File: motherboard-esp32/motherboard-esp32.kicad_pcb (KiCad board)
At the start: 4 copper layers, 123.8 x 77 mm, 41 parts, among them J2 Screw_Terminal_01x02, J3 JST_2P_XH, J4 JST_2P_XH, J5 Screw_Terminal_01x02, J6 Screw_Terminal_01x02, J7 XT60, P1 1.8mm_16AWG, P2 1.8mm_16AWG, P3 1.8mm_16AWG, P4 1.8mm_16AWG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

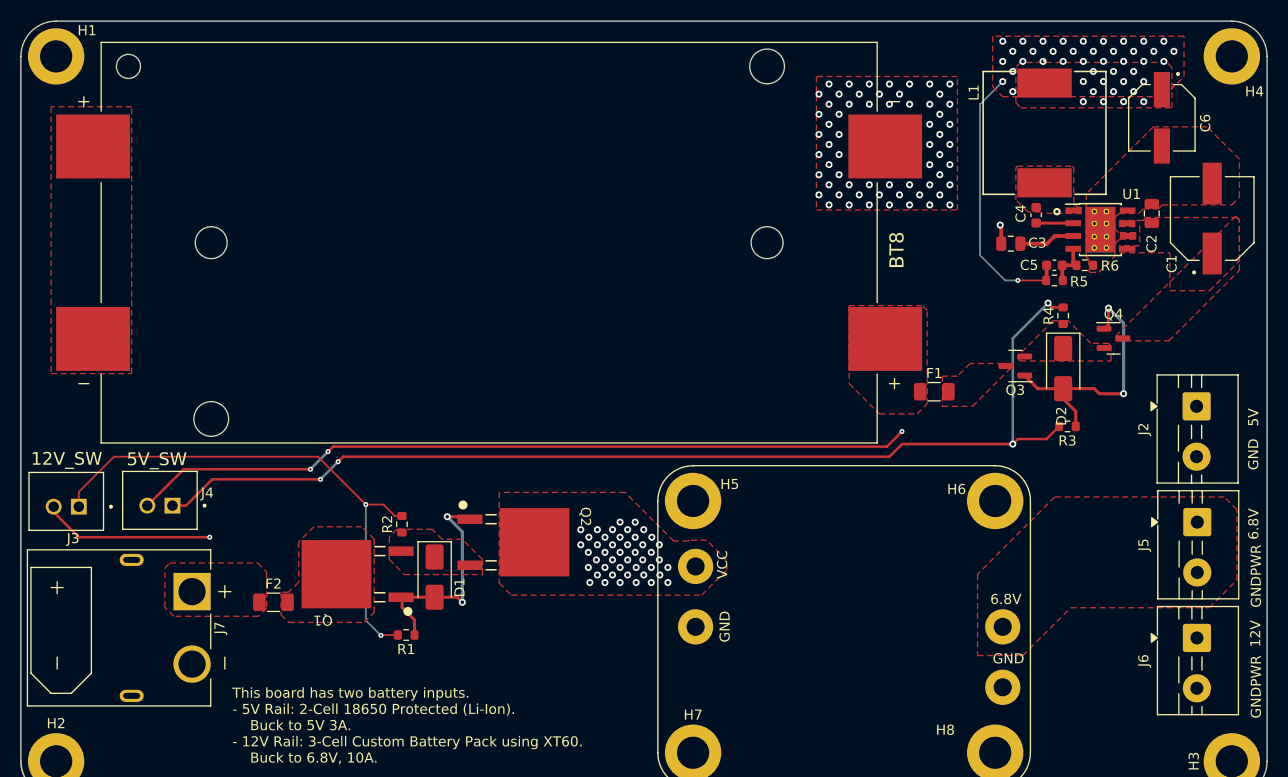
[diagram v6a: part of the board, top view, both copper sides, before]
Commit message: 5V 5A version
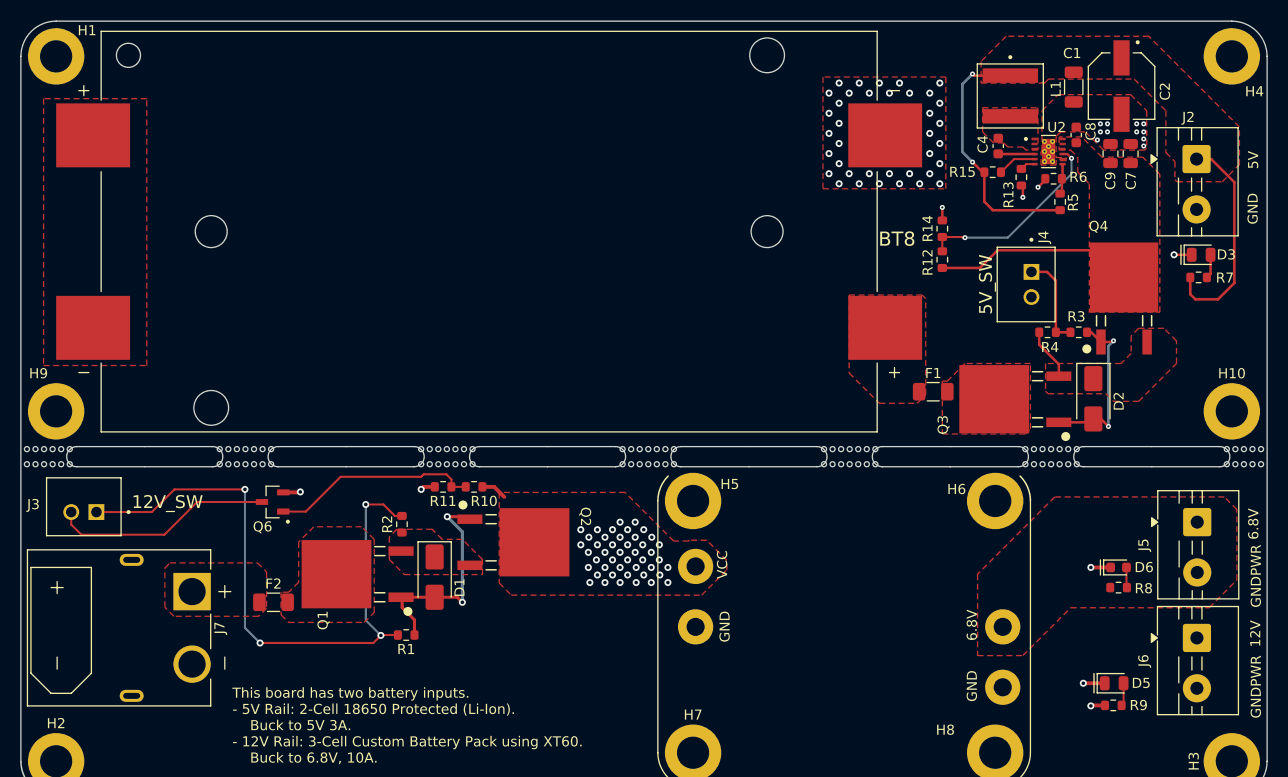
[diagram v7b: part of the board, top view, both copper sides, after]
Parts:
- removed C3: 2.2u, bio-robot:C_0805_2012Metric
- removed C5: 30p, bio-robot:C_0603_1608Metric
- removed C6: 16SVPF180M, bio-robot:CAP_16SVPF180M
- removed U1: LMR23630AFDDAR, bio-robot:TI_SO-PowerPAD-8_ThermalVias
- added B1: MouseBite, bio-robot:MouseBite-Long, F.Cu at (52.8, 61.8)
- added C7: 10u, bio-robot:C_0805_2012Metric, F.Cu at (160.7, 30.6)
- added C8: 0.1u, bio-robot:C_0603_1608Metric, F.Cu at (155.3, 28.8)
- added C9: 10u, bio-robot:C_0805_2012Metric, F.Cu at (158.7, 30.6)
- added D3: LED_green, bio-robot:LED_0805_2012Metric, F.Cu at (167.7, 40.7)
- added D5: LED_red, bio-robot:LED_0805_2012Metric, F.Cu at (159.1, 83.2)
- added D6: LED_blue, bio-robot:LED_0603_1608Metric, F.Cu at (159.5, 71.8)
- added H10: MountingHoleM3, bio-robot:MountingHole_3.2mm_M3_DIN965_Pad, F.Cu at (170.8, 56.2)
- added H9: MountingHoleM3, bio-robot:MountingHole_3.2mm_M3_DIN965_Pad, F.Cu at (54.0, 56.2)
- added Q6: TN2130K1-G, bio-robot:SOT95P240X111-3N, F.Cu at (75.5, 65.2)
- added R10: 11k, bio-robot:R_0603_1608Metric, F.Cu at (95.5, 63.8)
- added R11: 3.6k, bio-robot:R_0603_1608Metric, F.Cu at (92.4, 63.8)
- added R12: 698k, bio-robot:R_0603_1608Metric, F.Cu at (142.0, 41.2)
- added R13: 30.9k, bio-robot:R_0603_1608Metric, F.Cu at (149.8, 33.0)
- added R14: 200k, bots:R_0603_1608Metric, F.Cu at (142.0, 38.1)
- added R15: 100k, bots:R_0603_1608Metric, F.Cu at (147.0, 32.5)
- added R7: 3.3k, bio-robot:R_0603_1608Metric, F.Cu at (167.4, 43.0)
- added R8: 2k, bio-robot:R_0603_1608Metric, F.Cu at (159.5, 73.8)
- added R9: R_34k, bio-robot:R_0603_1608Metric, F.Cu at (159.0, 85.4)
- added U2: LMR51450SDRRR, bio-robot:CONV_LMR51450SDRRR, F.Cu at (152.6, 30.4)
- C1: value 25SVPF100M -> 22u_1206; footprint bio-robot:CAP_25SVPF100M -> bio-robot:C_1206_3216Metric
- C2: value 10u -> 10SVPC120M; footprint bio-robot:C_0805_2012Metric -> bio-robot:CAP_10SVPC120MV
- L1: value 27uH -> 4.7u; footprint bio-robot:IND_CDRH127_LDNP-470MC_SUM -> bio-robot:IND_XAL6060-472MEC
- Q3, Q4: value HL3415A -> DOD4185; footprint bio-robot:SOT-23 -> bots:DPAK-3_ONS
- R5: value 88.7k -> 100k; footprint bio-robot:R_0603_1608Metric -> bots:R_0603_1608Metric
- R6: value 22.1k -> 19.1k
- moved J4 88.7 mm to (150.3, 43.6), turned to 90 degrees
- moved J2 24.6 mm to (167.2, 31.2)
- moved C1 19.0 mm to (155.1, 24.1), turned to -90 degrees
- moved C2 13.0 mm to (159.8, 23.9), turned to -90 degrees
- moved R3 9.42 mm to (155.6, 48.4)
- moved R6 9.13 mm to (153.1, 33.1), turned to 180 degrees
- moved C4 7.83 mm to (147.6, 29.9)
- moved R5 7.82 mm to (153.7, 35.5), turned to -90 degrees
- moved Q4 6.14 mm to (160.1, 43.0)
- moved L1 5.00 mm to (148.8, 24.9)
- moved D2 4.24 mm to (157.0, 55.0)
- moved Q3 3.91 mm to (147.2, 55.0), turned to 90 degrees
- moved R4 2.26 mm to (152.4, 48.4), turned to 0 degrees
- moved J3 1.82 mm to (56.8, 65.7)
- moved BT8 1.10 mm to (97.0, 38.4)
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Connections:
- C1 pad 1: +BATT -> +5V
- C2 pad 1: +BATT -> +5V
- J3 pad 2: GNDPWR -> /Power Input/LV_D_VCC
- Q3 pad 2: /Power Input/BAT5V_MID -> /Power Input/FUSE_BAT5V
- Q3 pad 3: /Power Input/FUSE_BAT5V -> /Power Input/BAT5V_MID
- Q4 pad 2: /Power Input/BAT5V_MID -> +BATT
- Q4 pad 3: +BATT -> /Power Input/BAT5V_MID
- R5 pad 1: +5V -> /dc-dc/FB
- R5 pad 2: /dc-dc/FB -> +5V
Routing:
- net /Power Input/SW2: track 108.4 -> 9.36 mm, vias 4 -> 0
- net GND: track 79.9 -> 5.36 mm, vias 66 -> 52
- net /Power Input/LV_D_VCC: track 0.00 -> 22.0 mm
- net /Power Input/LV_G_VCC: track 0.00 -> 20.6 mm
- net +5V: track 27.3 -> 47.4 mm, vias 45 -> 2
- net +BATT: track 0.00 -> 19.9 mm
- net /dc-dc/EN: track 0.00 -> 19.5 mm, vias 0 -> 2
- net /Power Input/SW: track 52.8 -> 63.2 mm, vias 2 -> 4
- net GNDPWR: track 17.1 -> 7.25 mm, vias 1 -> 4
- net /Power Input/VGATE_2: track 26.2 -> 17.2 mm
- net /dc-dc/U1_VCC: track 5.57 -> 0.00 mm
- net /Power Input/BAT5V_MID: track 0.00 -> 5.16 mm
- net VCC: track 0.00 -> 4.01 mm, vias 45 -> 46
- net /dc-dc/PG: track 0.00 -> 3.87 mm
- net /Power Input/LED_5V: track 0.00 -> 2.40 mm
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- removed copper zone on In2.Cu, net +5V
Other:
- board text added: "Battery Motherboard MECH 540 / EECE 571M Marine Robotics Group 3: Quiet Bio-inspired Propulsion System Designed By: Henry Bryant Printed on: March 26th, 2026"
- board text removed: "Battery Motherboard MECH 540 / EECE 571M Marine Robotics Group 3: Quiet Bio-inspired Propulsion System Designed By: Henry Bryant Printed on: March 24th, 2026"

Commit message: ordered
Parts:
- added H11: MountingHoleM3, bio-robot:MountingHole_3.2mm_M3_DIN965_Pad, F.Cu at (115.8, 91.0)
- B1: value MouseBite -> Long_4mm_Attachment_no_mousebites; footprint bio-robot:MouseBite-Long -> bio-robot:Long_4mm_attachment_no_mouse_bites
- moved H5 6.70 mm to (124.0, 65.2)
- moved H7 6.70 mm to (124.0, 90.2)
- moved P1 6.70 mm to (124.2, 71.7)
- moved P2 6.70 mm to (124.2, 77.7)
- moved H6 6.70 mm to (153.9, 65.2)
- moved H8 6.70 mm to (153.9, 90.2)
- moved P3 6.70 mm to (154.7, 77.7)
- moved P4 6.70 mm to (154.7, 83.7)
- moved R8 3.17 mm to (161.7, 71.5), turned to 90 degrees
- moved R9 3.11 mm to (161.9, 84.4), turned to 90 degrees
- moved D5 1.28 mm to (159.7, 84.3), turned to 90 degrees
- moved D6 0.35 mm to (159.7, 71.5), turned to 90 degrees
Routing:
- net GNDPWR: track 7.25 -> 6.57 mm
